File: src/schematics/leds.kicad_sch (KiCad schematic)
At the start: 6 parts, among them Q3 NMOS, Q4 NMOS

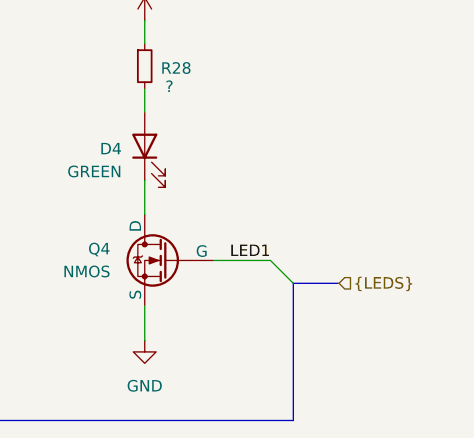
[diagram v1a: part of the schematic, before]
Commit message: Remove bus groups
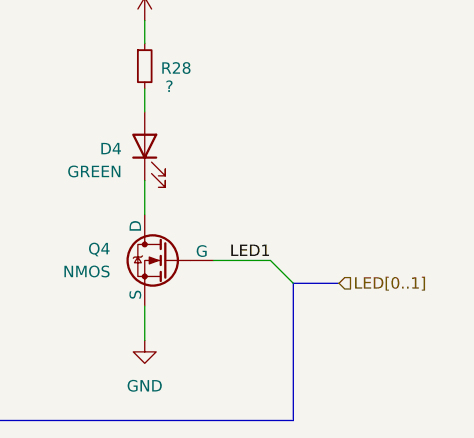
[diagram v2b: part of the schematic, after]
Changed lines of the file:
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@@
 		(comment 3 "${Part Number}")
-	)
-	(bus_alias "LEDS"
-		(members "LED0" "LED1")
 	)
 	(bus_entry
@@
 		)
 	)
-	(hierarchical_label "{LEDS}"
+	(hierarchical_label "LED[0..1]"
 		(shape input)
 		(at 179.07 104.14 0)

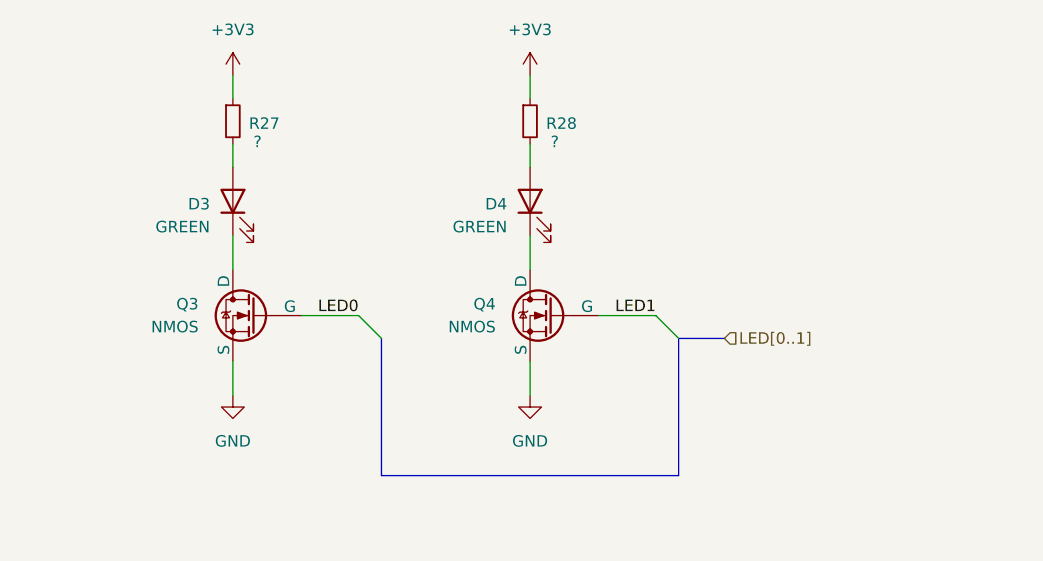
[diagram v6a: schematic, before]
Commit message: Add power good led
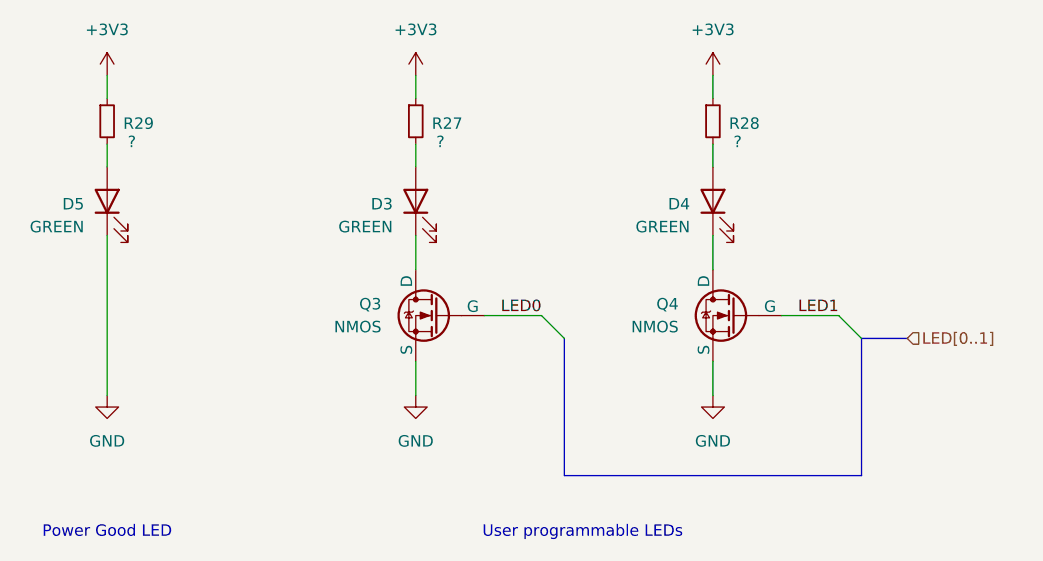
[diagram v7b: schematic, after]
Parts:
- added D5: GREEN, symbol Device:LED
- added R29: ?, symbol Device:R_Small
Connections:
- net +3V3: now also R29.1
- net GND: now also D5.1 (K)
- new net: D5.2 (A), R29.2
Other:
- note added: "Power Good LED"
- note added: "User programmable LEDs"
- moved on the sheet: D3, D4, Q3, Q4, R27, R28

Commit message: Add remaining component footprints (#79)
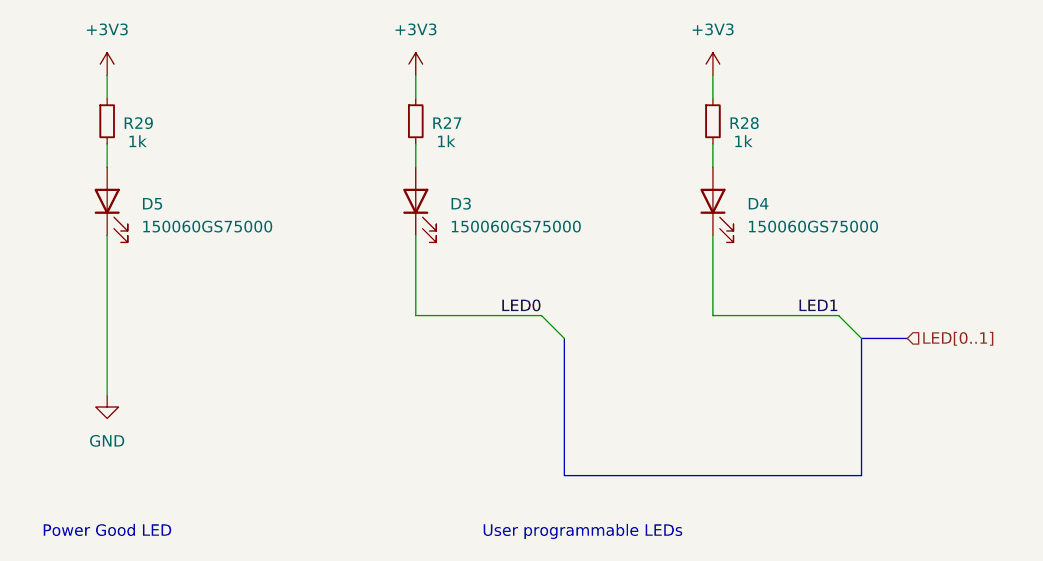
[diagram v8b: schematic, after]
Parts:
- removed Q3, Q4: NMOS, symbol Simulation_SPICE:NMOS
- D3, D4, D5: value GREEN -> 150060GS75000; footprint (none) -> LED_SMD:LED_0603_1608Metric
- R27, R28, R29: value ? -> 1k; footprint (none) -> Resistor_SMD:R_0603_1608Metric
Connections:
- net LED0: now also D3.1 (K)
- net LED1: now also D4.1 (K)
